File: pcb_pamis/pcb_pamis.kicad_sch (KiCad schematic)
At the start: 22 parts, among them J1 1755736, J2 USB_A, Q1 Q_NPN_BEC, Q2 Q_NPN_BEC, SW1 SW_Push, U1 ESP32-WROOM-32UE, U2 CP2102N-Axx-xQFN28

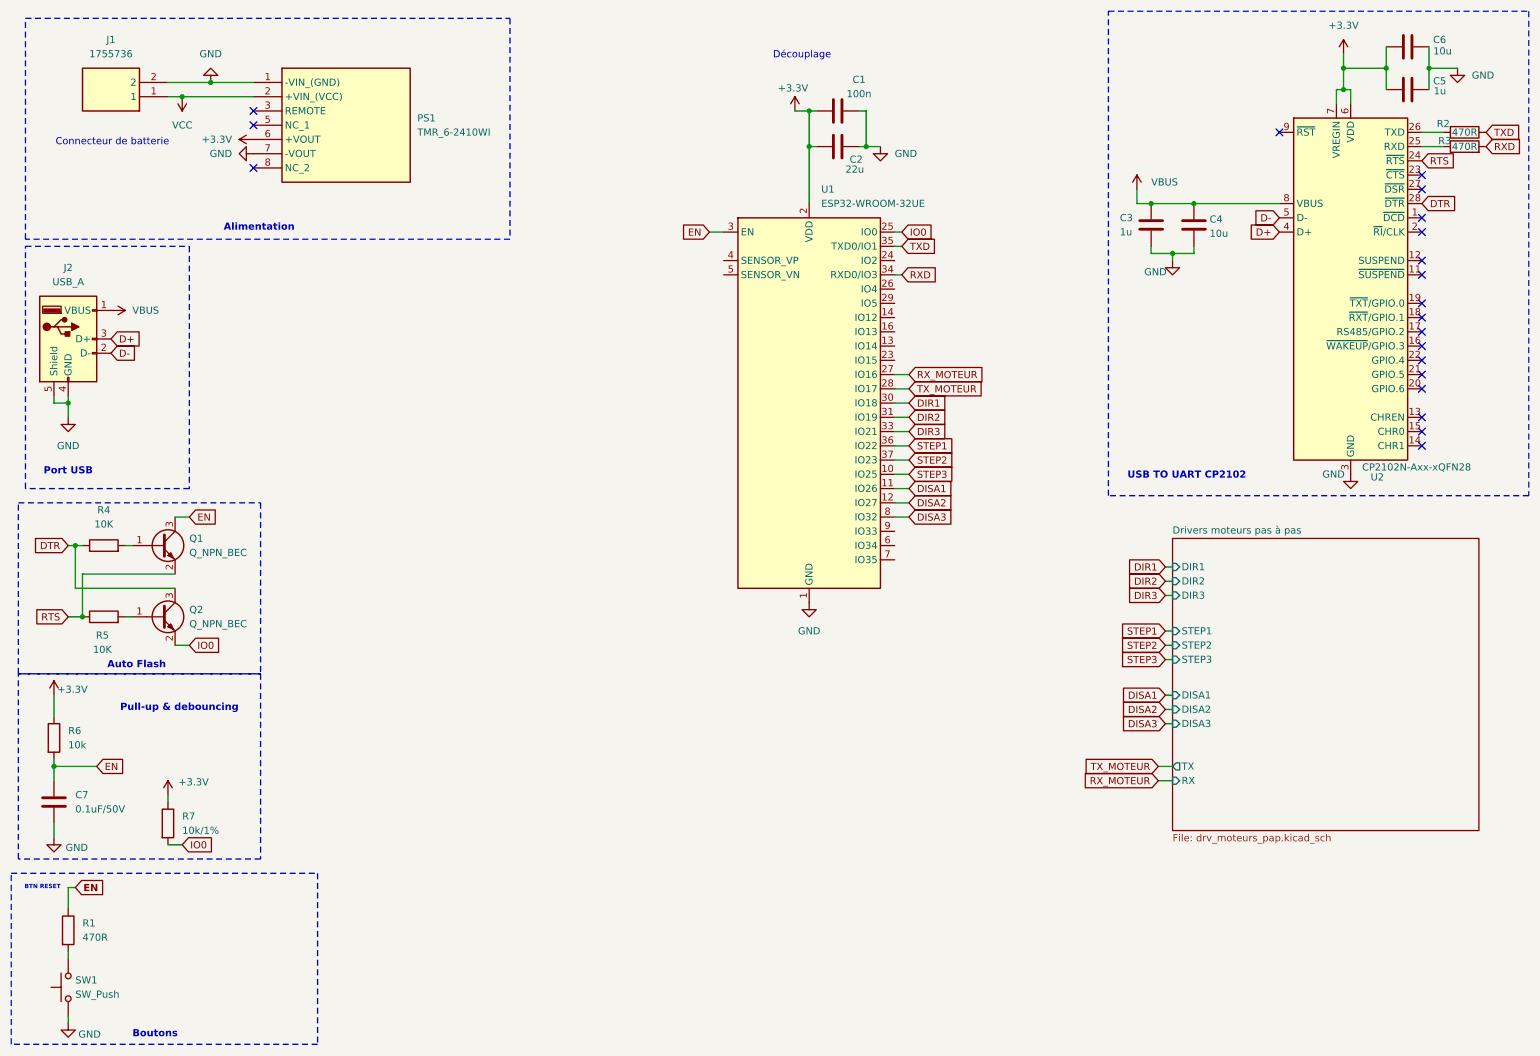
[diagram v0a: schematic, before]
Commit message: ajout bouton arrêt d'urgence
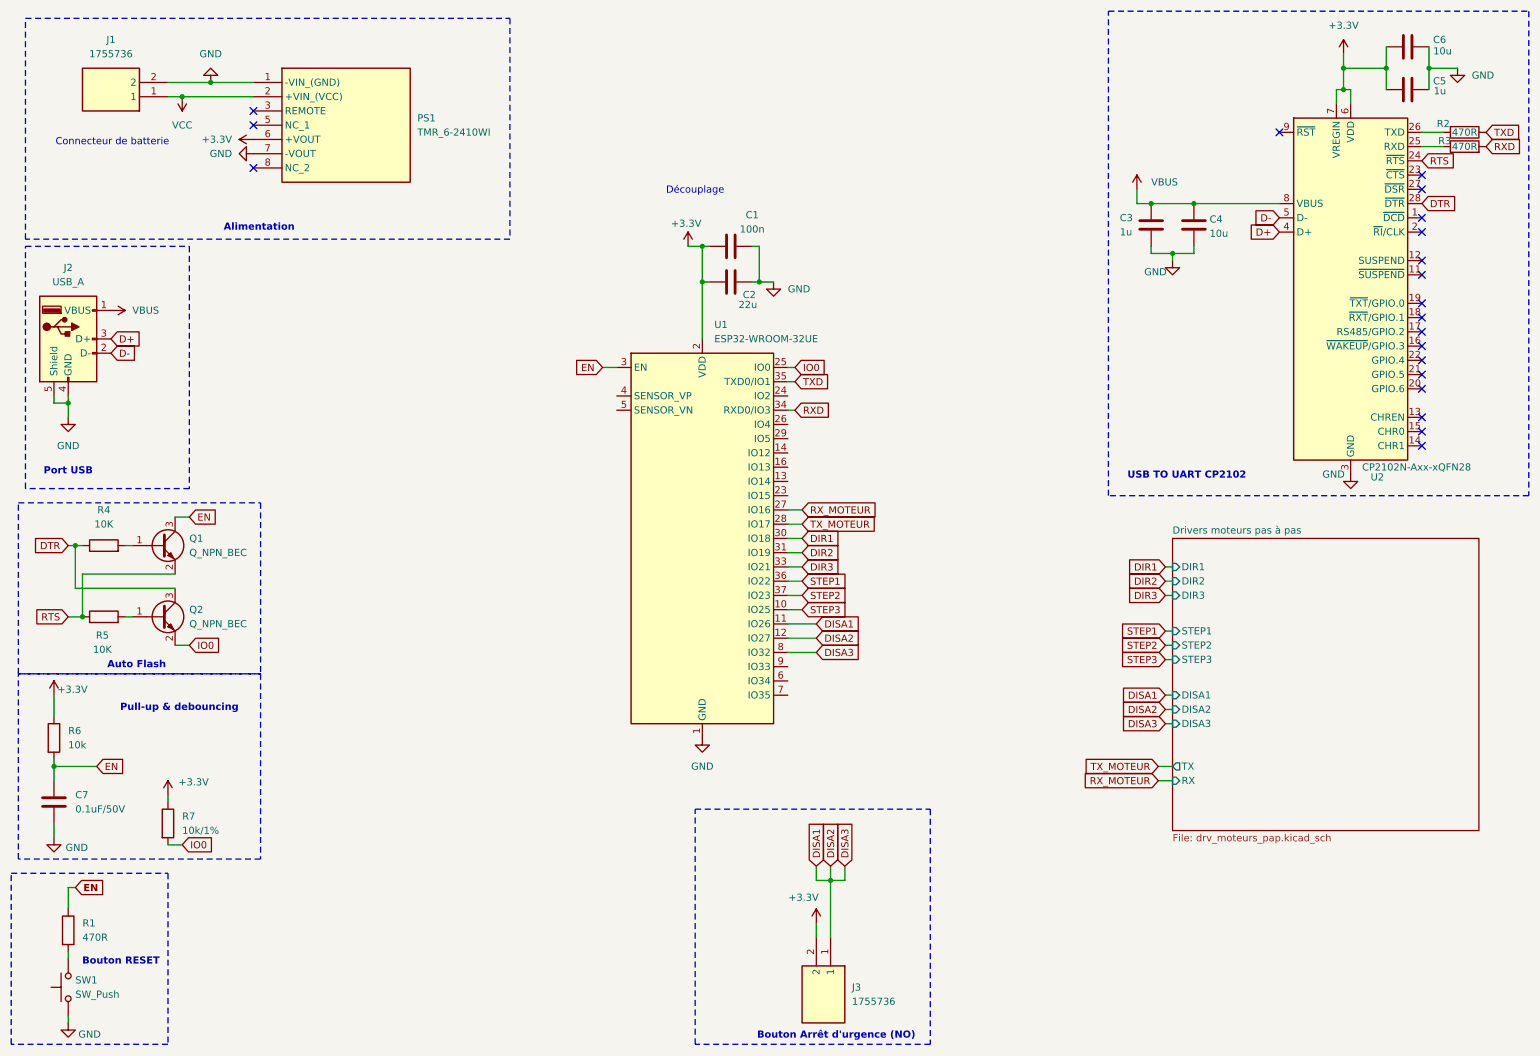
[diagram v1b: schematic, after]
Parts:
- added J3: 1755736, 1755736, symbol Modelec:1755736
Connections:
- net DISA2 is gone; now on net DISA1: U1.12 (IO27)
- net DISA3 is gone; now on net DISA1: U1.8 (IO32)
- net +3.3V: now also J3.2
- net DISA1: now also J3.1
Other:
- note added: "Bouton Arrêt d'urgence (NO)"
- note added: "Bouton RESET"
- note removed: "BTN RESET"
- note removed: "Boutons"
- moved on the sheet: C1, C2, U1

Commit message: ajustement pos pins pcb odometrie + 3 batteries et TODOs sur le schema pcb pamis
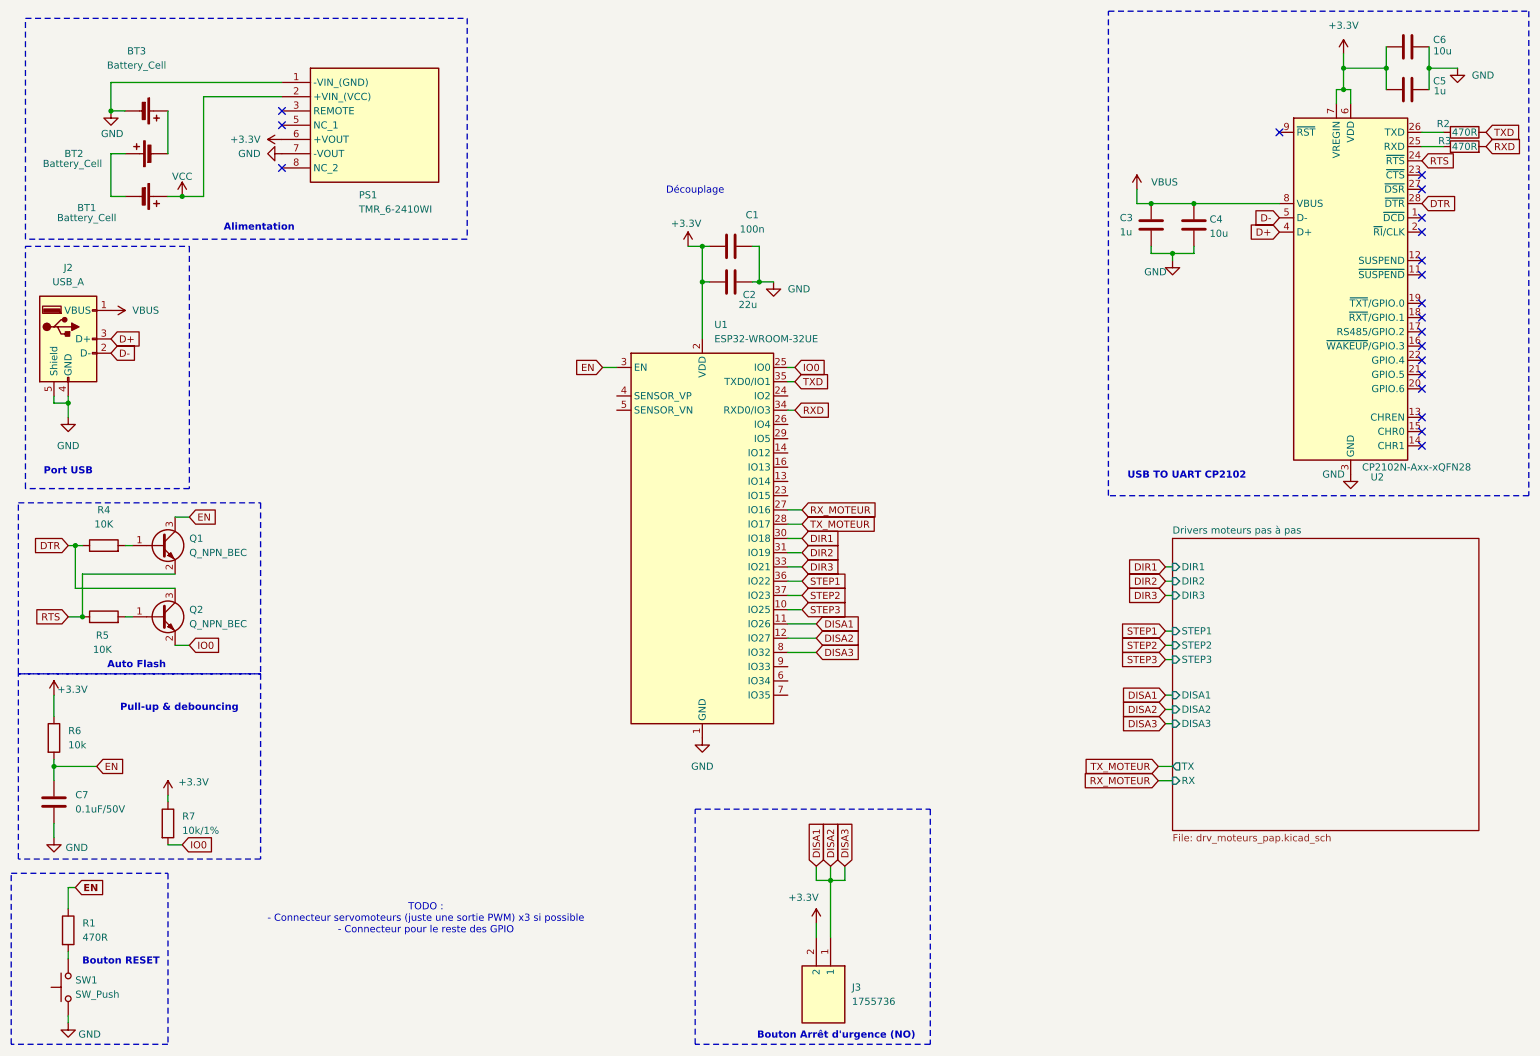
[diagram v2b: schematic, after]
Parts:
- removed J1: 1755736, Modelec:PhoenixContact_MSTBVA_2,5_2-G-5,08_1x02_P5.08mm_Vertical, symbol Modelec:1755736
- added BT1, BT2, BT3: Battery_Cell, symbol Device:Battery_Cell
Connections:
- net GND: now also BT3.2 (-)
- net VCC: now also BT1.1 (+)
- new net: BT2.2 (-), BT3.1 (+)
- new net: BT1.2 (-), BT2.1 (+)
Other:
- note added: "TODO : - Connecteur servomoteurs (juste une sortie PWM) x3 si possible - Connecteur pour le reste des GPIO"
- note removed: "Connecteur de batterie"
- moved on the sheet: PS1

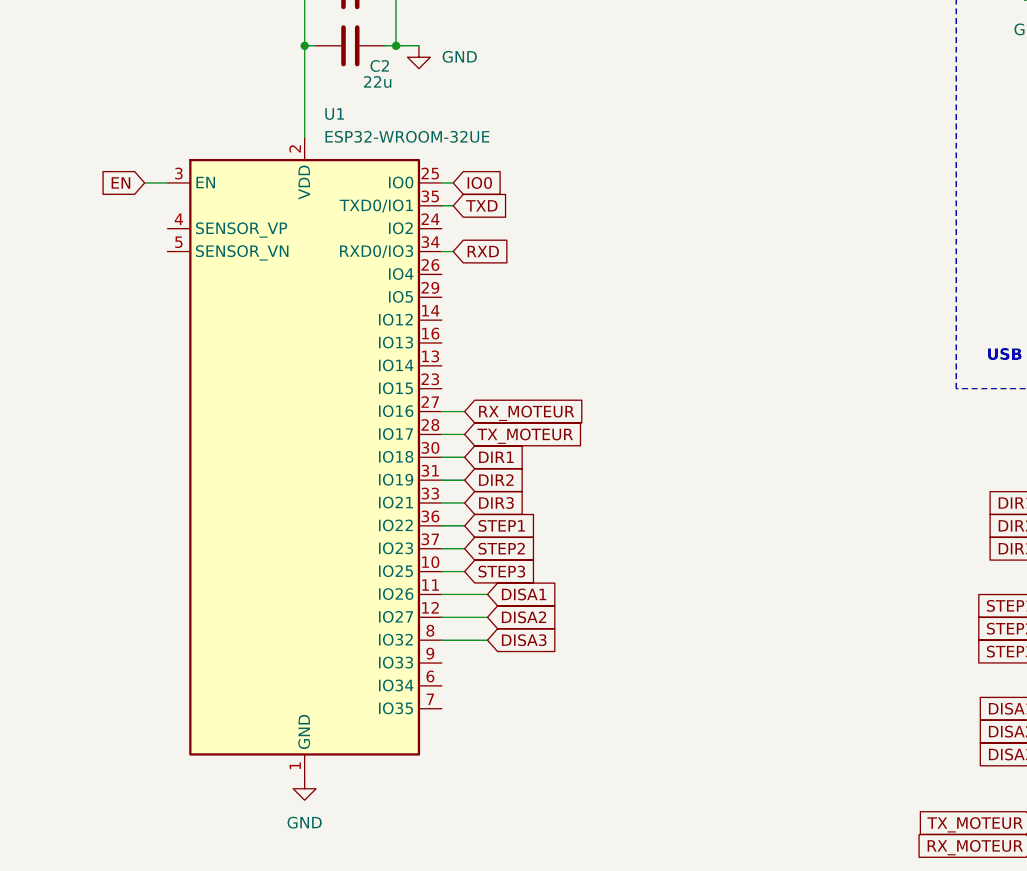
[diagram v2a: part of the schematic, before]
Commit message: ajout d'un connecteur pour les GPIO restant
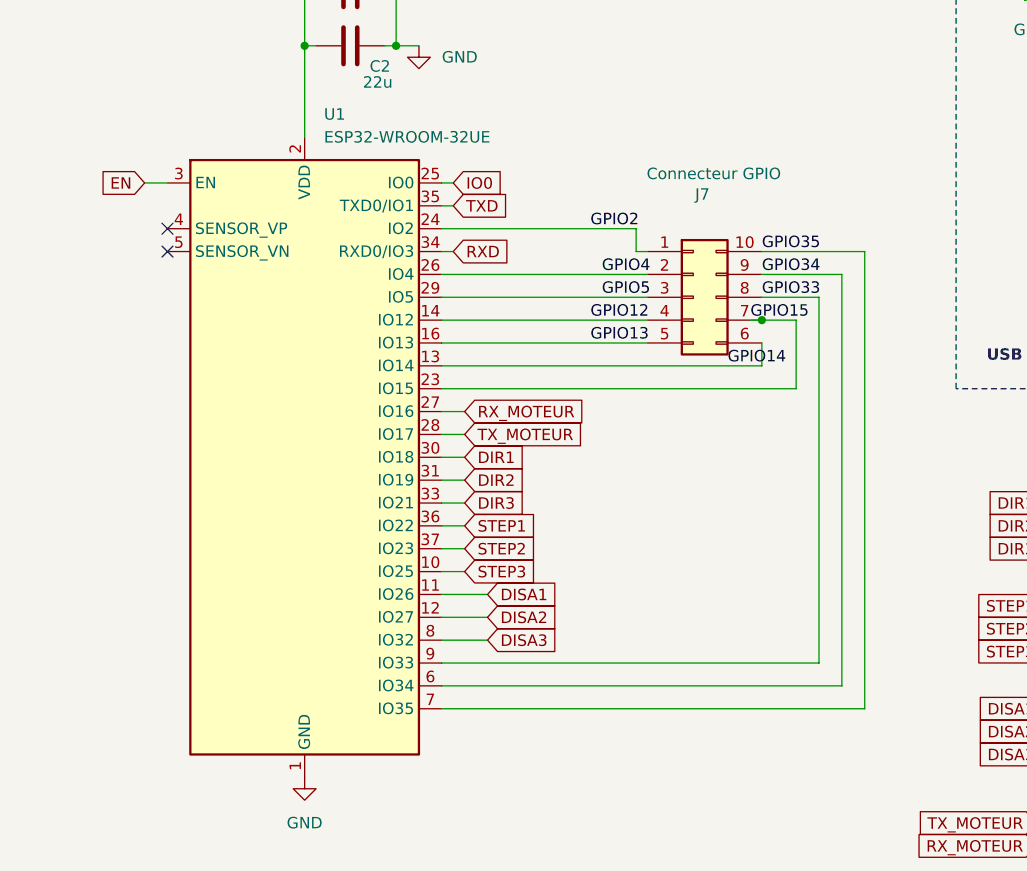
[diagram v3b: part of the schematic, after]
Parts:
- added J7: Connecteur GPIO, symbol Connector_Generic:Conn_02x05_Counter_Clockwise
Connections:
- net GPIO14: now reaches U1.13 (IO14)
- net GPIO14: now also J7.6 (Pin_6)
- net GPIO12: now reaches U1.14 (IO12)
- net GPIO12: now also J7.4 (Pin_4)
- net GPIO13: now reaches U1.16 (IO13)
- net GPIO13: now also J7.5 (Pin_5)
- net GPIO15: now reaches U1.23 (IO15)
- net GPIO15: now also J7.7 (Pin_7)
- net GPIO2: now reaches U1.24 (IO2)
- net GPIO2: now also J7.1 (Pin_1)
- net GPIO4: now reaches U1.26 (IO4)
- net GPIO4: now also J7.2 (Pin_2)
- net GPIO5: now reaches U1.29 (IO5)
- net GPIO5: now also J7.3 (Pin_3)
- net GPIO34: now reaches U1.6 (IO34)
- net GPIO34: now also J7.9 (Pin_9)
- net GPIO35: now reaches U1.7 (IO35)
- net GPIO35: now also J7.10 (Pin_10)
- net GPIO33: now reaches U1.9 (IO33)
- net GPIO33: now also J7.8 (Pin_8)
- no-connect marks 20 -> 22
